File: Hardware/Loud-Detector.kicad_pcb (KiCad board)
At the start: 2 copper layers, 26 parts, among them J1 TP4056, J2 ON_OFF, J3 VIN+, J4 VIN-, J5 VOUT+, J6 VOUT-, J7 KY-038, Q1 BC557, Q2 BC547, U1 ATtiny85-20P, U2 MT3608_Module

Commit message: Adding schematics, PCB layout and base firmware
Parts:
- added D2: LED, LED_THT:LED_D3.0mm_Horizontal_O3.81mm_Z6.0mm, F.Cu at (166.8, 86.7)
- J7: value KY-038 -> KY-037
- R1: value 1K -> 470
- R5: value 1K -> 2K
- RV2: value 10K -> 500
- moved C1 66.5 mm to (128.1, 113.4)
- moved C2 41.0 mm to (151.2, 112.4)
- moved C3 41.0 mm to (151.2, 116.5)
- moved Q1 36.9 mm to (164.7, 70.1)
- moved Q2 36.9 mm to (164.7, 75.9)
- moved D1 33.4 mm to (160.8, 86.7)
- moved J1 26.3 mm to (163.9, 101.3)
- moved J2 26.3 mm to (163.9, 107.2)
- moved J7 26.3 mm to (163.9, 113.0)
- moved U1 26.3 mm to (151.2, 100.8)
- moved U2 26.3 mm to (143.9, 76.4)
- moved J6 26.3 mm to (147.3, 114.8)
- moved BZ1 26.3 mm to (149.7, 91.8)
- moved H1 26.3 mm to (172.5, 101.2)
- moved H2 26.3 mm to (172.5, 106.3)
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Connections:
- BZ1 pad 1: +5V -> Net-(BZ1-+)
- R1 pad 1: +5V -> Net-(R1-Pad1)
- R1 pad 2: Net-(R1-Pad2) -> THRESHOLD
- R4 pad 1: +5V -> BUZZ+LED1
- R4 pad 2: Net-(R4-Pad2) -> Net-(Q2-B)
- R5 pad 1: BUZZ+LED -> BUZZ+LED1
- R5 pad 2: Net-(Q2-B) -> Net-(D1-A)
- R6 pad 1: BUZZ+LED -> LED2
- R6 pad 2: Net-(D1-A) -> Net-(D2-A)
- RV1 pad 1: Net-(R1-Pad2) -> +5V
- RV1 pad 2: THRESHOLD -> Net-(R1-Pad1)
- RV2 pad 1: Net-(R4-Pad2) -> unconnected-(RV2-Pad1)
- RV2 pad 2: VOLUME -> Net-(BZ1-+)
- RV2 pad 3: GND -> +5V
- U1 pad 2: VOLUME -> LED2
- U1 pad 6: BUZZ+LED -> BUZZ+LED1

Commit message: Adding schematics, PCB layout and base firmware
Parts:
- removed BZ1: Buzzer, Buzzer_Beeper:Buzzer_TDK_PS1240P02BT_D12.2mm_H6.5mm
- added J8: BUZZER, Connector_JST:JST_EH_B2B-EH-A_1x02_P2.50mm_Vertical, F.Cu at (166.4, 87.3)
- J7: footprint Connector_JST:JST_EH_B4B-EH-A_1x04_P2.50mm_Vertical -> Connector_JST:JST_EH_B3B-EH-A_1x03_P2.50mm_Vertical
- R3, R4: footprint Resistor_THT:R_Axial_DIN0207_L6.3mm_D2.5mm_P2.54mm_Vertical -> Resistor_THT:R_Axial_DIN0207_L6.3mm_D2.5mm_P7.62mm_Horizontal
- U1: value ATtiny85-20P -> ATtiny85
- moved C1 61.9 mm to (167.0, 65.3), turned to 90 degrees
- moved H2 61.0 mm to (116.8, 81.3)
- moved J1 59.8 mm to (118.1, 62.9), turned to -90 degrees
- moved J2 57.5 mm to (118.1, 72.4), turned to -90 degrees
- moved J6 51.6 mm to (157.1, 64.1)
- moved H1 50.8 mm to (137.8, 64.1)
- moved J4 46.3 mm to (126.6, 64.1)
- moved Q1 44.1 mm to (128.9, 95.9)
- moved RV2 42.0 mm to (168.9, 102.1), turned to 90 degrees
- moved C3 40.6 mm to (127.0, 83.9), turned to -90 degrees
- moved J7 40.4 mm to (132.1, 88.2), turned to 90 degrees
- moved J5 39.4 mm to (157.1, 72.0)
- moved J3 35.6 mm to (126.6, 72.0)
- moved C2 33.1 mm to (149.3, 79.4)
- moved U1 25.2 mm to (137.8, 79.4)
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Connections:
- C3 pad 2: Net-(J7-Pin_2) -> Net-(J7-Pin_1)
- J1 pad 1: VBAT+ -> VIN-
- J1 pad 2: VIN- -> VBAT+
- J7 pad 1: unconnected-(J7-Pin_1-Pad1) -> Net-(J7-Pin_1)
- J7 pad 2: Net-(J7-Pin_2) -> GND
- J7 pad 3: GND -> MIC_OUT
- Q1 pad 1: Net-(J7-Pin_2) -> Net-(J7-Pin_1)
- RV1 pad 1: +5V -> GND
- RV1 pad 3: GND -> +5V
- RV2 pad 1: unconnected-(RV2-Pad1) -> +5V
- RV2 pad 3: +5V -> unconnected-(RV2-Pad3)
- U1 pad 2: LED2 -> THRESHOLD
- U1 pad 3: THRESHOLD -> MIC_OUT
- U1 pad 7: MIC_OUT -> LED2
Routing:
- net +5V: track 0.00 -> 150.0 mm, vias 0 -> 2
- net GND: track 0.00 -> 145.2 mm, vias 0 -> 5
- net THRESHOLD: track 0.00 -> 20.8 mm
- net LED2: track 0.00 -> 15.9 mm
- net BUZZ+LED1: track 0.00 -> 14.4 mm
- net Net-(Q1-B): track 0.00 -> 12.9 mm
- net Net-(J7-Pin_1): track 0.00 -> 11.7 mm
- net Net-(Q2-B): track 0.00 -> 11.6 mm
- net Net-(J8-Pin_2): track 0.00 -> 10.8 mm
- net VIN+: track 0.00 -> 9.69 mm
- net VIN-: track 0.00 -> 9.02 mm
- net VBAT+: track 0.00 -> 7.03 mm
- net MIC_OUT: track 0.00 -> 6.24 mm
- net Net-(R1-Pad1): track 0.00 -> 5.30 mm
- net Net-(D1-A): track 0.00 -> 4.97 mm
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- added copper zone on B.Cu, net GND
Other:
- board outline added: 59.7 x 47.6 mm

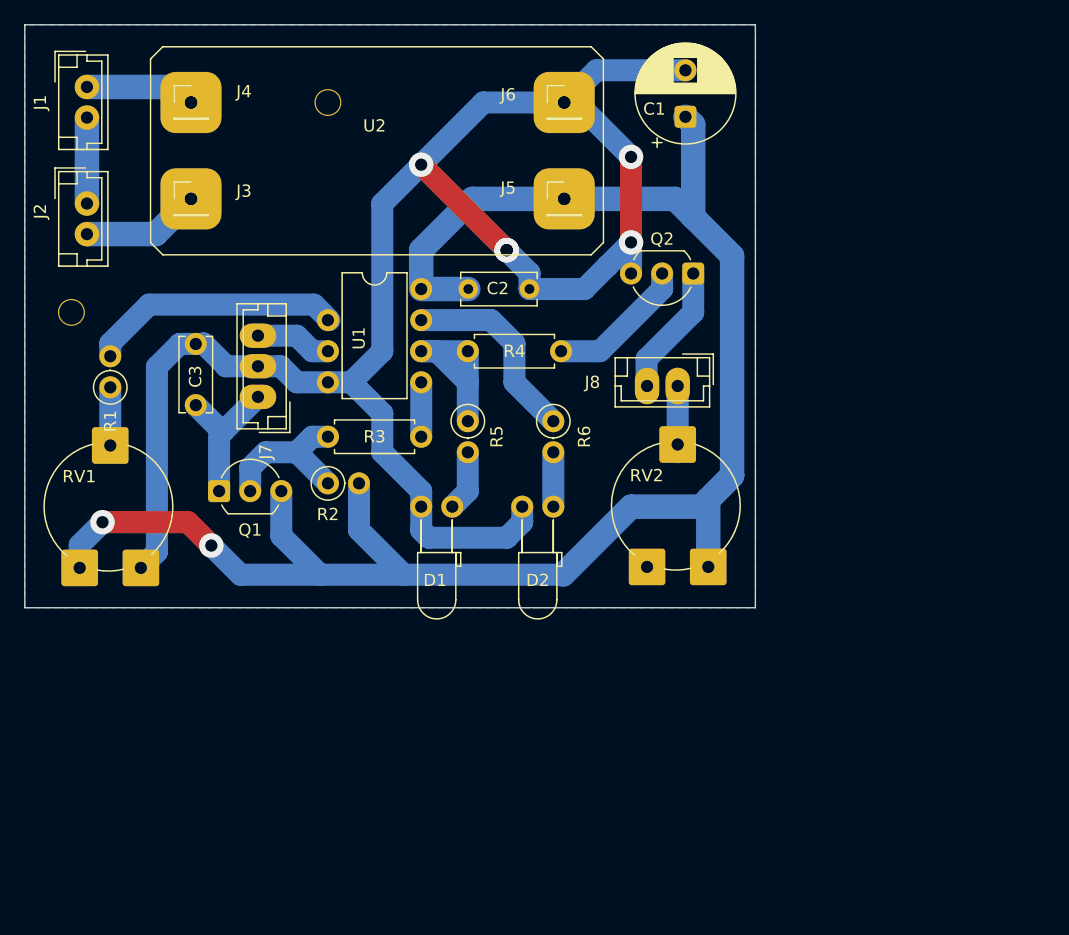
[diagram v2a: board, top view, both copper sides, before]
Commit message: Adding case 3D model
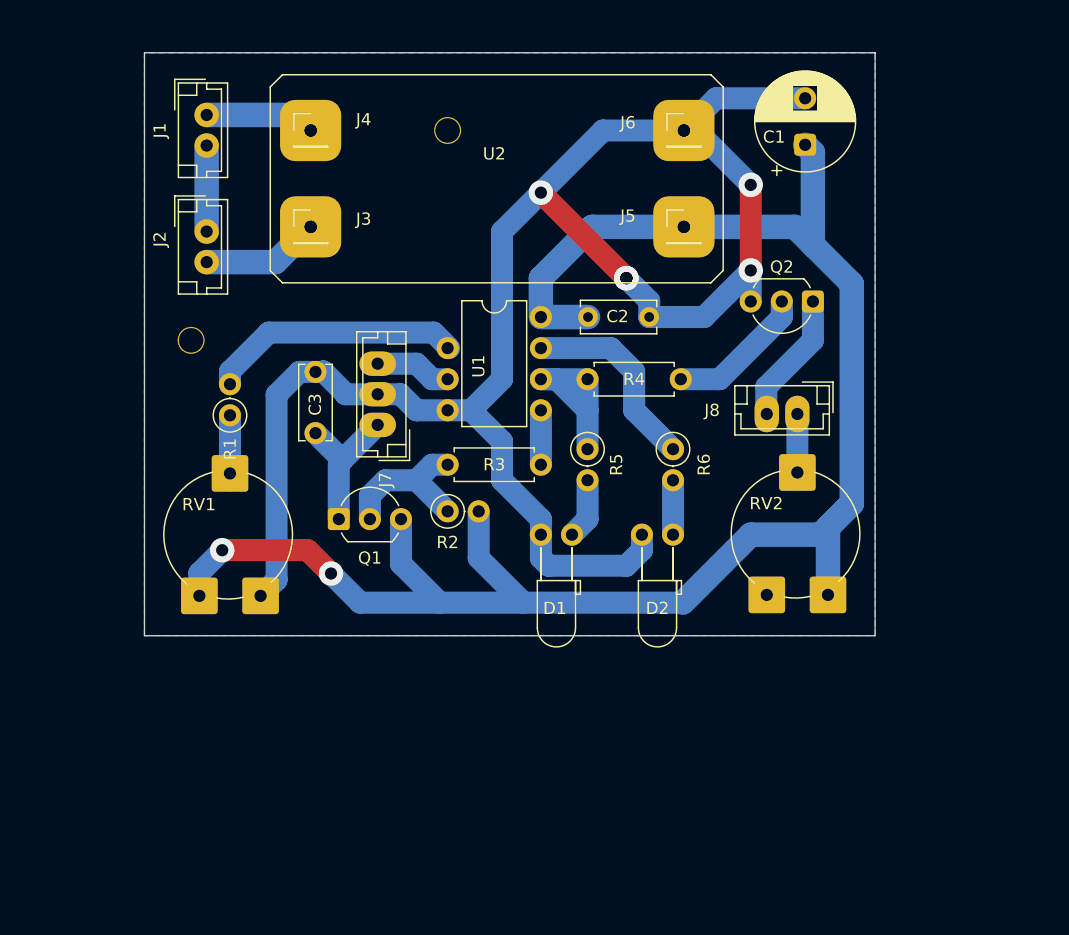
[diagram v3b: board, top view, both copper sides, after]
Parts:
- moved C2 10.0 mm to (159.0, 81.7)
- moved D2 10.0 mm to (163.4, 99.4)
- moved H1 10.0 mm to (147.6, 66.4)
- moved Q2 10.0 mm to (177.4, 80.4)
- moved R2 10.0 mm to (147.6, 97.5)
- moved U1 10.0 mm to (147.6, 81.7)
- moved R1 10.0 mm to (129.8, 89.7)
- moved RV1 10.0 mm to (132.3, 104.4)
- moved C1 10.0 mm to (176.8, 67.6)
- moved C3 10.0 mm to (136.8, 86.1)
- moved D1 10.0 mm to (155.2, 99.4)
- moved H2 10.0 mm to (126.6, 83.6)
- moved J2 10.0 mm to (127.9, 74.7)
- moved J3 10.0 mm to (136.4, 74.3)
- moved J4 10.0 mm to (136.4, 66.4)
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
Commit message: PCB minor improvements
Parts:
- RV1: value 10K -> 5K
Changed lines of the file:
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@@
 			)
 		)
-		(property "Value" "10K"
+		(property "Value" "5K"
 			(at 5 0.525 90)
 			(layer "F.Fab")
@@
 	)
 	(zone
-		(net 12)
-		(net_name "Net-(R1-Pad1)")
+		(net 19)
+		(net_name "Net-(J8-Pin_1)")
 		(layer "B.Cu")
 		(name "$teardrop_padvia$")
 		(hatch none 0.1)
-		(priority 30000)
+		(priority 30001)
 		(attr
 			(teardrop
@@
 		(polygon
 			(pts
-				(xy 130.694 91.941) (xy 128.894 91.941) (xy 128.794 92.941) (xy 129.794 94.442) (xy 130.794 92.941)
+				(xy 177.049 91.861) (xy 175.249 91.861) (xy 175.149 92.861) (xy 176.149 94.362) (xy 177.149 92.861)
 			)
 		)
 	)
 	(zone
-		(net 19)
-		(net_name "Net-(J8-Pin_1)")
+		(net 2)
+		(net_name "+5V")
 		(layer "B.Cu")
 		(name "$teardrop_padvia$")
@@
 		(polygon
 			(pts
-				(xy 177.049 91.861) (xy 175.249 91.861) (xy 175.149 92.861) (xy 176.149 94.362) (xy 177.149 92.861)
+				(xy 128.379408 102.763383) (xy 127.106617 101.490592) (xy 126.566162 102.941) (xy 127.293293 104.441707)
+				(xy 128.601343 102.952406)
 			)
 		)
 	)
 	(zone
-		(net 1)
-		(net_name "GND")
+		(net 12)
+		(net_name "Net-(R1-Pad1)")
 		(layer "B.Cu")
-		(name "GND")
-		(hatch edge 0.5)
+		(name "$teardrop_padvia$")
+		(hatch none 0.1)
+		(priority 30000)
+		(attr
+			(teardrop
+				(type padvia)
+			)
+		)
 		(connect_pads yes
-			(clearance 1)
+			(clearance 0)
 		)
-		(min_thickness 0.25)
+		(min_thickness 0.0254)
 		(filled_areas_thickness no)
 		(fill yes
 			(thermal_gap 0.5)
 			(thermal_bridge_width 0.5)
+			(island_removal_mode 1)
+			(island_area_min 10)
 		)
 		(polygon
 			(pts
-				(xy 122.809 60.071) (xy 122.809 107.696) (xy 182.499 107.696) (xy 182.499 60.071)
+				(xy 130.694 91.941) (xy 128.894 91.941) (xy 128.794 92.941) (xy 129.794 94.442) (xy 130.794 92.941)
 			)
 		)
 	)
 	(zone
-		(net 2)
-		(net_name "+5V")
+		(net 1)
+		(net_name "GND")
 		(layer "B.Cu")
-		(name "$teardrop_padvia$")
-		(hatch none 0.1)
-		(priority 30002)
-		(attr
-			(teardrop
-				(type padvia)
-			)
-		)
+		(name "GND")
+		(hatch edge 0.5)
 		(connect_pads yes
-			(clearance 0)
+			(clearance 1)
 		)
-		(min_thickness 0.0254)
+		(min_thickness 0.25)
 		(filled_areas_thickness no)
 		(fill yes
 			(thermal_gap 0.5)
 			(thermal_bridge_width 0.5)
-			(island_removal_mode 1)
-			(island_area_min 10)
 		)
 		(polygon
 			(pts
-				(xy 128.379408 102.763383) (xy 127.106617 101.490592) (xy 126.566162 102.941) (xy 127.293293 104.441707)
-				(xy 128.601343 102.952406)
+				(xy 122.809 60.071) (xy 122.809 107.696) (xy 182.499 107.696) (xy 182.499 60.071)
 			)
 		)

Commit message: PCB minor improvements
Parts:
- RV1: value 5K -> 10K
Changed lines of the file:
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@@
 			)
 		)
-		(property "Value" "5K"
+		(property "Value" "10K"
 			(at 5 0.525 90)
 			(layer "F.Fab")
@@
 	)
 	(segment
+		(start 140.429 104.996)
+		(end 138.049 102.616)
+		(width 1.8)
+		(layer "B.Cu")
+		(net 2)
+	)
+	(segment
 		(start 172.339 99.441)
 		(end 178.054 99.441)
@@
 	)
 	(segment
-		(start 140.429 104.996)
-		(end 146.939 104.996)
-		(width 1.8)
-		(layer "B.Cu")
-		(net 2)
-	)
-	(segment
-		(start 138.049 102.616)
+		(start 146.939 104.996)
 		(end 140.429 104.996)
 		(width 1.8)
@@
 	)
 	(segment
+		(start 146.939 104.996)
+		(end 146.845 104.902)
+		(width 1.8)
+		(layer "B.Cu")
+		(net 2)
+	)
+	(segment
 		(start 180.594 96.901)
 		(end 178.649 98.846)
@@
 	)
 	(zone
-		(net 19)
-		(net_name "Net-(J8-Pin_1)")
+		(net 2)
+		(net_name "+5V")
 		(layer "B.Cu")
 		(name "$teardrop_padvia$")
@@
 		(polygon
 			(pts
-				(xy 177.049 91.861) (xy 175.249 91.861) (xy 175.149 92.861) (xy 176.149 94.362) (xy 177.149 92.861)
+				(xy 128.379408 102.763383) (xy 127.106617 101.490592) (xy 126.566162 102.941) (xy 127.293293 104.441707)
+				(xy 128.601343 102.952406)
 			)
 		)
 	)
 	(zone
-		(net 2)
-		(net_name "+5V")
+		(net 19)
+		(net_name "Net-(J8-Pin_1)")
 		(layer "B.Cu")
 		(name "$teardrop_padvia$")
@@
 		(polygon
 			(pts
-				(xy 128.379408 102.763383) (xy 127.106617 101.490592) (xy 126.566162 102.941) (xy 127.293293 104.441707)
-				(xy 128.601343 102.952406)
+				(xy 177.049 91.861) (xy 175.249 91.861) (xy 175.149 92.861) (xy 176.149 94.362) (xy 177.149 92.861)
 			)
 		)
@@
 			)
 		)
+	)
+	(zone
+		(net 12)
+		(net_name "Net-(R1-Pad1)")
+		(layer "B.Cu")
+		(name "$teardrop_padvia$")
+		(hatch none 0.1)
+		(priority 30002)
+		(attr
+			(teardrop
+				(type padvia)
+			)
+		)
+		(connect_pads yes
+			(clearance 0)
+		)
+		(min_thickness 0.0254)
+		(filled_areas_thickness no)
+		(fill yes
+			(thermal_gap 0.5)
+			(thermal_bridge_width 0.5)
+			(island_removal_mode 1)
+			(island_area_min 10)
+		)
+		(polygon
+			(pts
+				(xy 128.379408 102.763383) (xy 127.106617 101.490592) (xy 126.566162 102.941) (xy 127.293293 104.441707)
+				(xy 128.601343 102.952406)
+			)
+		)
